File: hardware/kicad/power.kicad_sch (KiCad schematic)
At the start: 0 parts

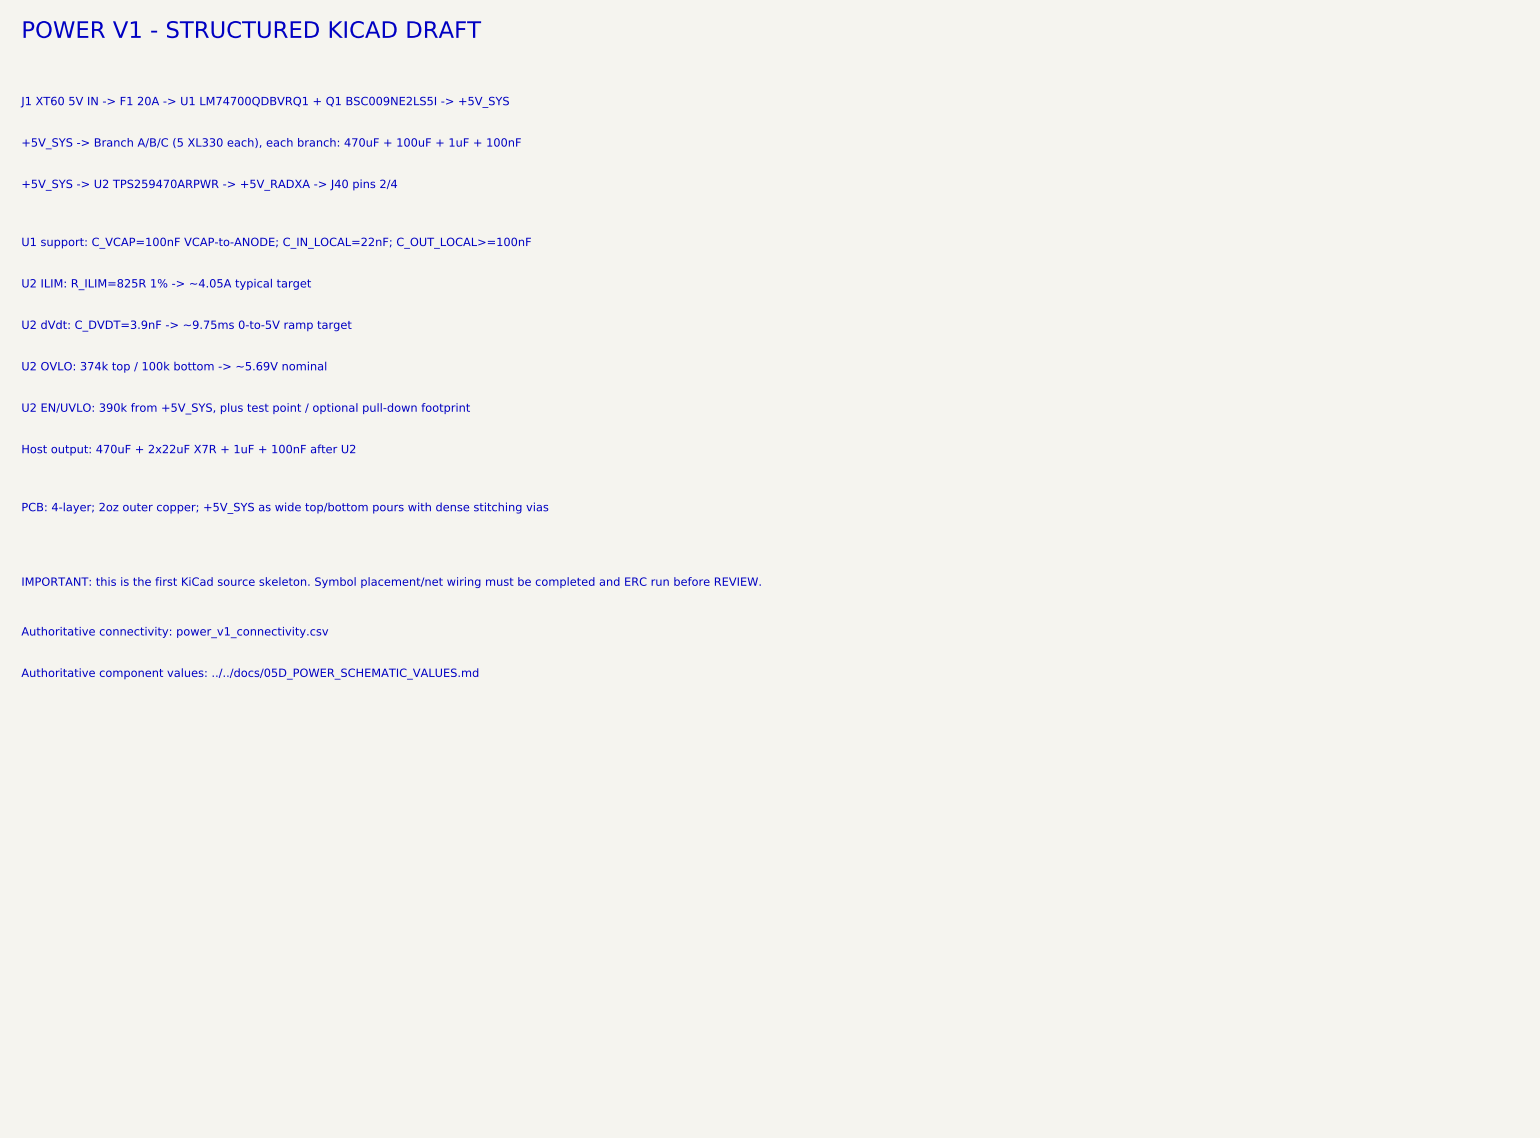
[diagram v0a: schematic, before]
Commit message: [verified] refactor(hardware): restore strict single-board Radxa port
Import the routed upstream Pollen Robot HAT as the active design, adapt the critical host nets for Radxa ZERO 3W, remove the divergent high-current redesign artifacts, and add regenerated baseline-aware KiCad validation.
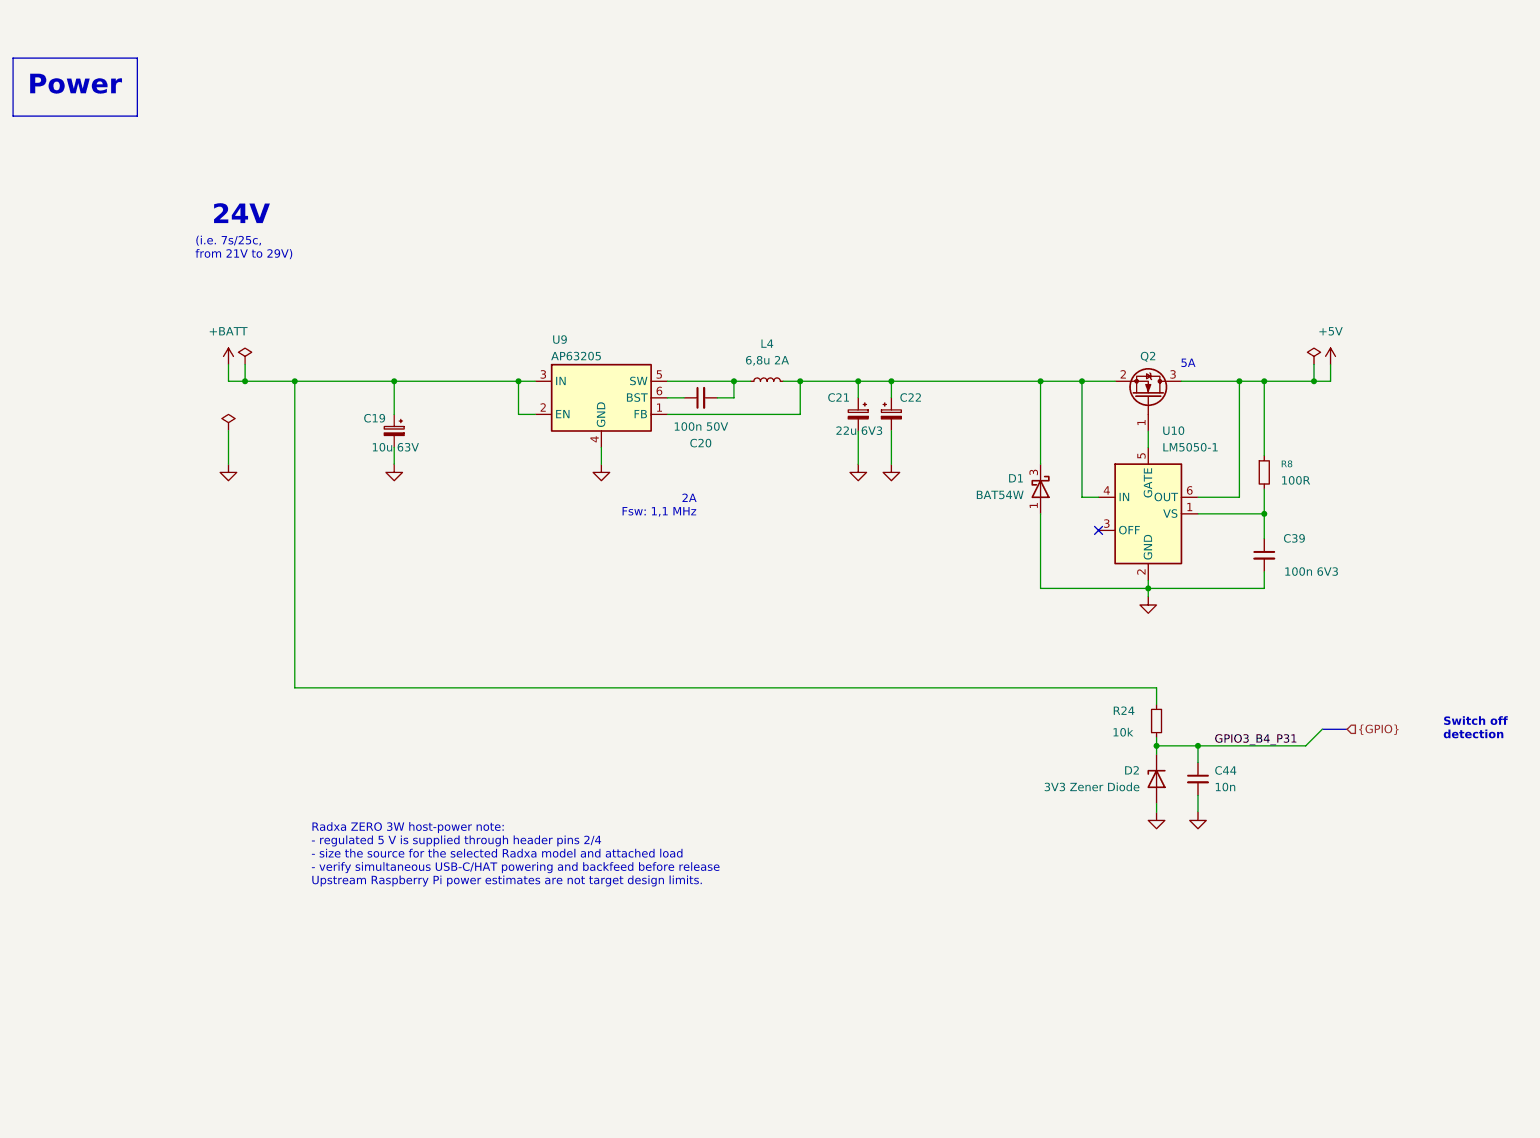
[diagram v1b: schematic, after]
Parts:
- added C19: 10u 63V, Capacitor_SMD:CP_Elec_6.3x7.7, symbol Device:C_Polarized_Small
- added C20: 100n 50V, Capacitor_SMD:C_0402_1005Metric, symbol Device:C_Small
- added C21, C22: 22u 6V3, Capacitor_SMD:C_0603_1608Metric, symbol Device:C_Polarized_Small
- added C39: 100n 6V3, Capacitor_SMD:C_0402_1005Metric, symbol Device:C_Small
- added C44: 10n, Capacitor_SMD:C_0402_1005Metric, symbol Device:C_Small
- added D1: BAT54W, Package_TO_SOT_SMD:SOT-323_SC-70, symbol Diode:BAT54W
- added D2: 3V3 Zener Diode, Diode_SMD:D_SOD-123, symbol Device:D_Zener
- added L4: 6,8u 2A, Inductor_SMD:L_Bourns_SRN6045TA, symbol Device:L_Small
- added Q2: SI2312CDS-T1-GE3, Package_TO_SOT_SMD:TSOT-23, symbol Transistor_FET_Other:Q_NMOS_Depletion_GSD
- added R24: 10k, Resistor_SMD:R_0402_1005Metric, symbol Device:R_Small
- added R8: 100R, Resistor_SMD:R_0402_1005Metric, symbol Device:R_Small
- added U10: LM5050-1, Package_TO_SOT_SMD:TSOT-23-6, symbol Power_Management:LM5050-1
- added U9: AP63205, Package_TO_SOT_SMD:TSOT-23-6, symbol Regulator_Switching:AP63205WU
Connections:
- new net: C39.1, R8.2, U10.1 (VS)
- new net: C21.1, C22.1, D1.3 (K), L4.1, Q2.2 (S), U10.4 (IN), U9.1 (FB)
- new net: Q2.1 (G), U10.5 (GATE)
- new net: C20.2, L4.2, U9.5 (SW)
- new net: C20.1, U9.6 (BST)
- new net +5V: Q2.3 (D), R8.1, U10.6 (OUT)
- new net +BATT: C19.1, R24.2, U9.2 (EN), U9.3 (IN)
- new net GND: C19.2, C21.2, C22.2, C39.2, C44.2, D1.1 (A), D2.2 (A), U10.2 (GND), U9.4 (GND)
- new net GPIO3_B4_P31: C44.1, D2.1 (K), R24.1
- no-connect marks 0 -> 1
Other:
- note added: "(i.e. 7s/25c, from 21V to 29V)"
- note added: "24V"
- note added: "2A Fsw: 1,1 MHz"
- note added: "5A"
- note added: "Radxa ZERO 3W host-power note: - regulated 5 V is supplied through header pins 2/4 - size the source for the selected Radxa model and attached load - verify simultaneous USB-C/HAT powering and backfeed before release Upstream Raspberry Pi power estimates are not target design limits."
- note added: "Switch off detection"
- note removed: "+5V_SYS -> Branch A/B/C (5 XL330 each), each branch: 470uF + 100uF + 1uF + 100nF"
- note removed: "+5V_SYS -> U2 TPS259470ARPWR -> +5V_RADXA -> J40 pins 2/4"
- note removed: "Authoritative component values: ../../docs/05D_POWER_SCHEMATIC_VALUES.md"
- note removed: "Authoritative connectivity: power_v1_connectivity.csv"
- note removed: "Host output: 470uF + 2x22uF X7R + 1uF + 100nF after U2"
- note removed: "IMPORTANT: this is the first KiCad source skeleton. Symbol placement/net wiring must be completed and ERC run before REVIEW."
- note removed: "J1 XT60 5V IN -> F1 20A -> U1 LM74700QDBVRQ1 + Q1 BSC009NE2LS5I -> +5V_SYS"
- note removed: "PCB: 4-layer; 2oz outer copper; +5V_SYS as wide top/bottom pours with dense stitching vias"
- note removed: "POWER V1 - STRUCTURED KICAD DRAFT"
- note removed: "U1 support: C_VCAP=100nF VCAP-to-ANODE; C_IN_LOCAL=22nF; C_OUT_LOCAL>=100nF"
- note removed: "U2 EN/UVLO: 390k from +5V_SYS, plus test point / optional pull-down footprint"
- note removed: "U2 ILIM: R_ILIM=825R 1% -> ~4.05A typical target"
- note removed: "U2 OVLO: 374k top / 100k bottom -> ~5.69V nominal"
- note removed: "U2 dVdt: C_DVDT=3.9nF -> ~9.75ms 0-to-5V ramp target"
- company: juper007 / DIY -> Pollen Robotics / Hugging Face
- title: Radxa ZERO 3W Robot HAT - Power V1 -> Radxa ZERO 3W Robot HAT

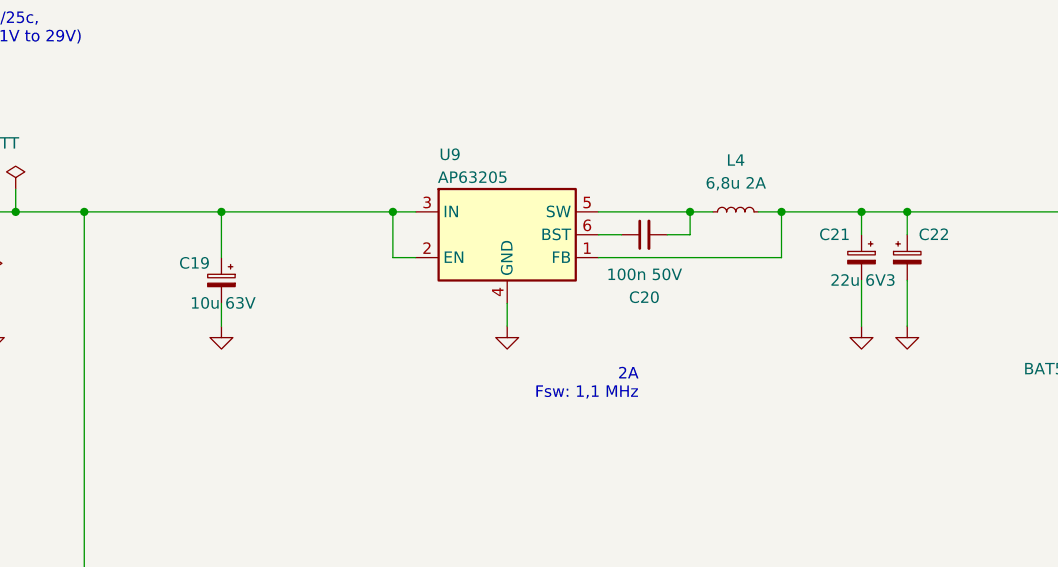
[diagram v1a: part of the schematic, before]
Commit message: [verified] fix(power): add C45 bypass and mechanical gates
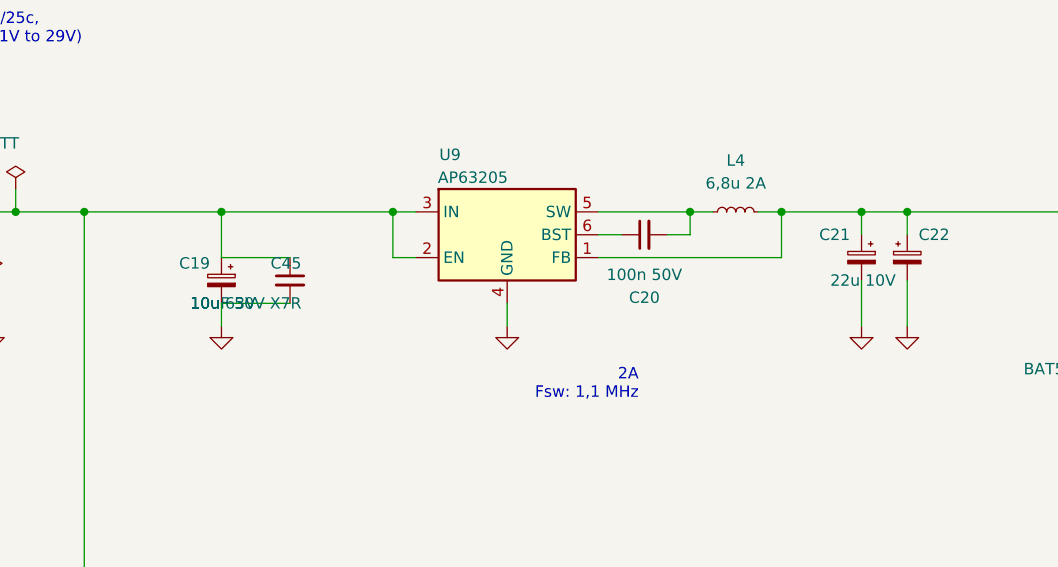
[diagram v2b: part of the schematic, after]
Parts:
- added C45: 10uF 50V X7R, Capacitor_SMD:C_1210_3225Metric, symbol Device:C_Small
- C21, C22: value 22u 6V3 -> 22u 10V
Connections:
- net +BATT: now also C45.1
- net GND: now also C45.2

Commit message: [verified] fix(hardware): correct power bias and default-off GPIO controls
Qualify Q2 land and gate rating, battery-bias LM5050 VS, and correct C39 identity. Add host-referenced active-low battery sensing and default-off amplifier control while preserving connector parity. Expand exact regression guards and complete BOM/position exports. Fabrication approval remains pending physical and runtime validation.
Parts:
- removed D2: 3V3 Zener Diode, Diode_SMD:D_SOD-123, symbol Device:D_Zener
- added Q3: BC847B, Package_TO_SOT_SMD:SOT-23, symbol Transistor_BJT:Q_NPN_BEC
- added R42: 100k, Resistor_SMD:R_0402_1005Metric, symbol Device:R_Small
- added R43: 10k, Resistor_SMD:R_0402_1005Metric, symbol Device:R_Small
- C39: value 100n 6V3 -> 100nF 50V X7R; Dielectric (none) -> X7R; LCSC Part C1525 -> (none); Man. (none) -> Samsung Electro-Mechanics; Man. Ref. (none) -> CL05B104KB5NNNC; Manufacturer_Name (none) -> Samsung Electro-Mechanics; Manufacturer_Part_Number (none) -> CL05B104KB5NNNC; Tolerance (none) -> 10%; Voltage Rating (none) -> 50V
- Q2: value SI2312CDS-T1-GE3 -> DMN3023L-7; footprint Package_TO_SOT_SMD:TSOT-23 -> Package_TO_SOT_SMD:DMN3023L_SOT23_Diodes; symbol Transistor_FET_Other:Q_NMOS_Depletion_GSD -> Transistor_FET:Q_NMOS_GSD; LCSC Part C142518 -> C443825; Manufacturer_Name (none) -> Diodes Incorporated; Manufacturer_Part_Number (none) -> DMN3023L-7
- R24: value 10k -> 100k; LCSC Part C25744 -> (none); Length 1.6 -> (none); Manufacturer_Name (none) -> Yageo; Manufacturer_Part_Number (none) -> RC0402FR-07100KL; Power Rating (none) -> 0.063W; Tolerance (none) -> 1%; Voltage Rating (none) -> 50V; Width 0.9 -> (none)
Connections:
- net +5V: no longer R8.1
- net +BATT: now also R8.1
- net GND: now also Q3.2 (E), R42.2
- net GPIO3_B4_P31: now also Q3.3 (C), R43.1; no longer R24.1
- new net +3V3: R43.2
- new net BAT_BASE: Q3.1 (B), R24.1, R42.1
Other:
- note added: "2A path"
- note added: "2S Li-ion input"
- note added: "Battery present = LOW; collector referenced to host 3V3"
- note added: "NP-F550 style 2S Li-ion Nominal 7.2-7.4V; assumed max 8.4V Assumed minimum 6.0V; not a BMS guarantee Exact battery SKU confirmation required"
- note removed: "(i.e. 7s/25c, from 21V to 29V)"
- note removed: "24V"
- note removed: "5A"
